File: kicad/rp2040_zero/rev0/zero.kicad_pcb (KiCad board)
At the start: 2 copper layers, 41.8 x 30.2 mm, 18 parts, among them J1 jtag, J2 Conn_01x03_Socket, J5 Debug port, U1 RP2040-Zero, U3 3V->VTREF, U4 VTREF->3V, U5 VTREF<->3V, U6 RT9013-33GB

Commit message: cleanup
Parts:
- removed kibuzzard-66C04372: G***, kibuzzard-66C04372
- removed kibuzzard-66C0437E: G***, kibuzzard-66C0437E
- added .: PinHeader_1x01_P2.54mm_Vertical, Connector_PinHeader_2.54mm:PinHeader_1x01_P2.54mm_Vertical, F.Cu at (118.2, 68.8)
- added kibuzzard-6719D5E3: G***, kibuzzard-6719D5E3, F.Cu at (118.2, 81.1)
- added kibuzzard-6719D5F3: G***, kibuzzard-6719D5F3, F.Cu at (118.2, 71.5)
- added kibuzzard-6719D670: G***, kibuzzard-6719D670, F.Cu at (117.3, 73.2)
- added kibuzzard-6719D703: G***, kibuzzard-6719D703, F.Cu at (119.4, 95.7)
- added kibuzzard-6719D73B: G***, kibuzzard-6719D73B, F.Cu at (133.0, 73.3)
- moved C3 1.07 mm to (120.8, 69.2), turned to -90 degrees
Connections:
- U1 pad 19: OUT_SWDCLK_3V -> OUT_SWDIO_3V
- U1 pad 20: OUT_SWDIO_3V -> OUT_SWDCLK_3V
- U1 pad 7: unconnected-(U1-GP26-Pad7) -> INOUT_NRESET
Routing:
- net INOUT_NRESET: track 65.8 -> 49.9 mm, vias 3 -> 2
- net OUT_SWDCLK_3V: track 7.04 -> 11.0 mm, vias 0 -> 2
- net +3.3V: track 55.1 -> 55.6 mm
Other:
- board text removed: "NRESET-ADC: TODO"

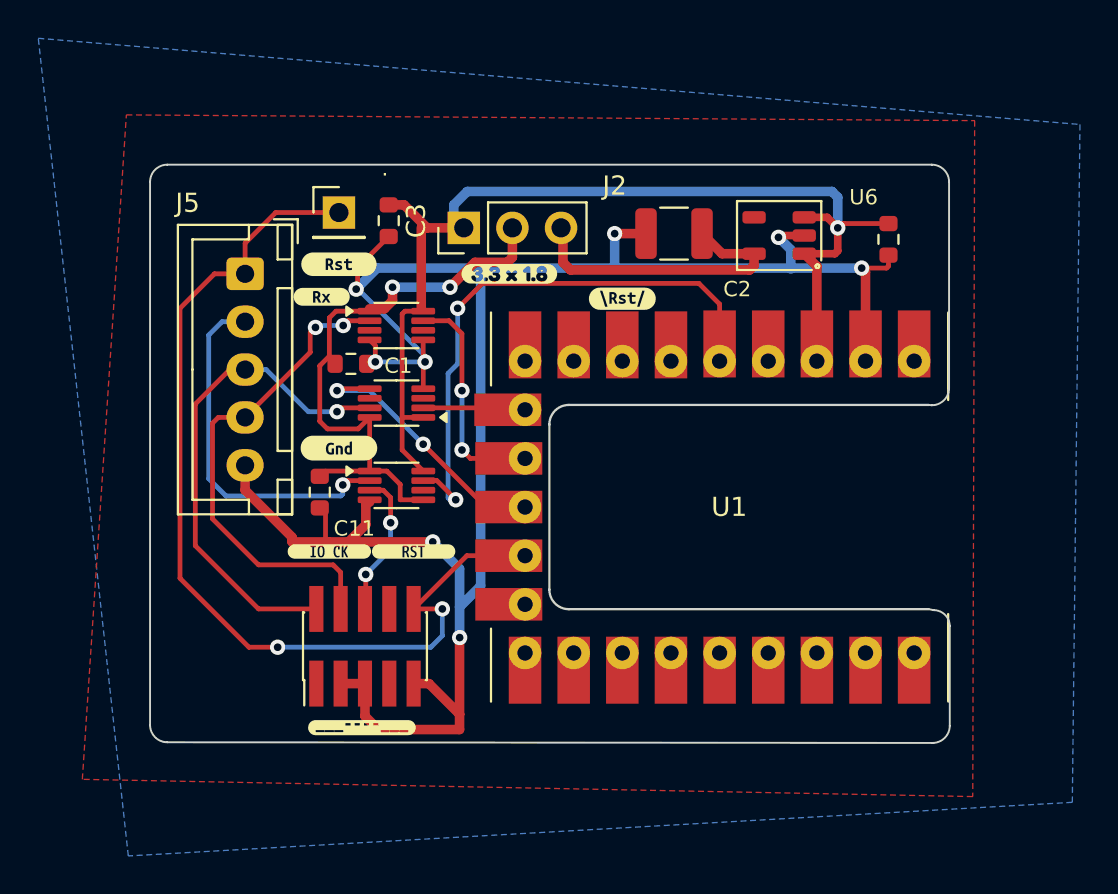
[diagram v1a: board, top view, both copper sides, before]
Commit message: RP2040 : Add USE_RP2040 option to use the new PCB Kicad : RP2040 carrier layout mon : add mon enablereset to make exec from RAM work with vscode. That ignores the reset command sent by cortexdebug Misc : dont hardcode the target in the attach/vAttch command to 1.  Actually read the value.
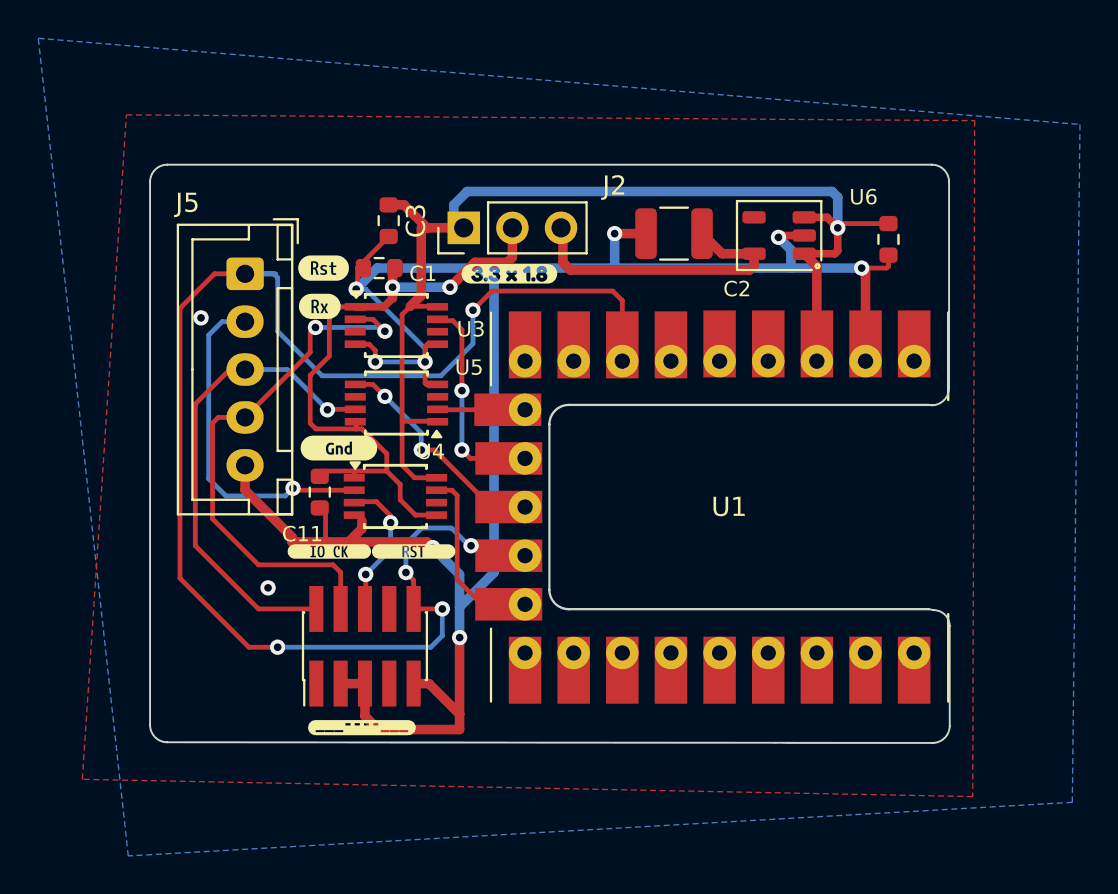
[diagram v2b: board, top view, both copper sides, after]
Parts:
- removed .: PinHeader_1x01_P2.54mm_Vertical, Connector_PinHeader_2.54mm:PinHeader_1x01_P2.54mm_Vertical
- removed kibuzzard-6719D5F3: G***, kibuzzard-6719D5F3
- removed kibuzzard-6719D670: G***, kibuzzard-6719D670
- removed kibuzzard-6719D73B: G***, kibuzzard-6719D73B
- added kibuzzard-67310D89: G***, kibuzzard-67310D89, F.Cu at (117.4, 71.7)
- added kibuzzard-67310DA4: G***, kibuzzard-67310DA4, F.Cu at (117.2, 73.7)
- U3, U4, U5: footprint Package_SO:VSSOP-8_2.3x2mm_P0.5mm -> Package_SO:TSSOP-8_3x3mm_P0.65mm
- moved C1 5.21 mm to (120.3, 71.7), turned to 180 degrees
- moved U4 0.58 mm to (121.2, 83.6)
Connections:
- U1 pad 23: unconnected-(U1-GP9-Pad23) -> OUT_UART_RX_3V
- U1 pad 5: OUT_UART_RX_3V -> unconnected-(U1-GP28-Pad5)
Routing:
- net INOUT_NRESET: track 49.9 -> 76.1 mm, vias 2 -> 5
- net OUT_UART_RX_3V: track 29.3 -> 7.41 mm, vias 2 -> 0
- net VTREF: track 30.2 -> 33.0 mm
- net OUT_SWDCLK: track 25.8 -> 28.3 mm
- net +3.3V: track 55.6 -> 57.7 mm
- net SWIO_DIR_3V: track 12.0 -> 10.3 mm
- net OUT_UART_RX: track 19.1 -> 18.1 mm
- net OUT_SWDIO: track 25.1 -> 24.3 mm
- net OUT_SWDIO_3V: track 4.31 -> 3.49 mm
- net GND: track 111.4 -> 112.1 mm, vias 8 -> 10
- net OUT_SWDCLK_3V: track 11.0 -> 10.3 mm
